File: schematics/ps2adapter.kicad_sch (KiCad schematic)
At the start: 8 parts, among them J14 PS/2, J15 port, U12 CD74HCT299E, U13 CD74HCT299E, U14 SN74LS14N

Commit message: Fix errors in schematics
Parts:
- removed C6: CAP, symbol pspice:CAP
- removed D8: DIODE, symbol pspice:DIODE
- added C2: C, symbol Device:C
- added D8: D, symbol Device:D
- renumbered J14 to J12, J15 to J13
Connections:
- net GND: now also C2.2
- net at R14.1, U14.2 (1Y): now also D8.2 (A)
- net at R14.2, U14.3 (2A): now also C2.1, D8.1 (K)

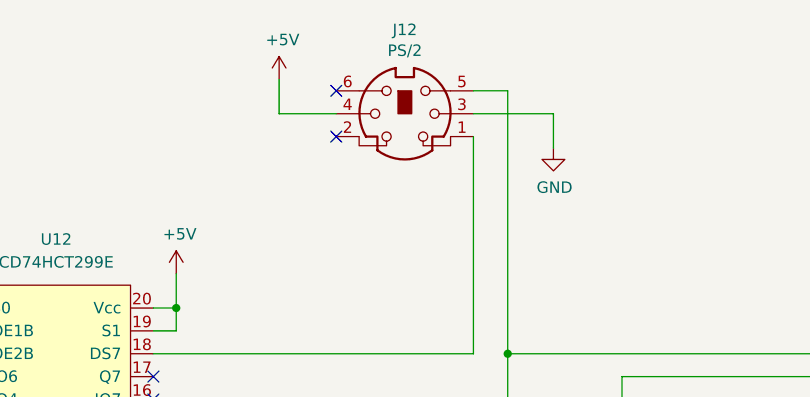
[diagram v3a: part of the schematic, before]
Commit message: Update schematics for latest KiCad
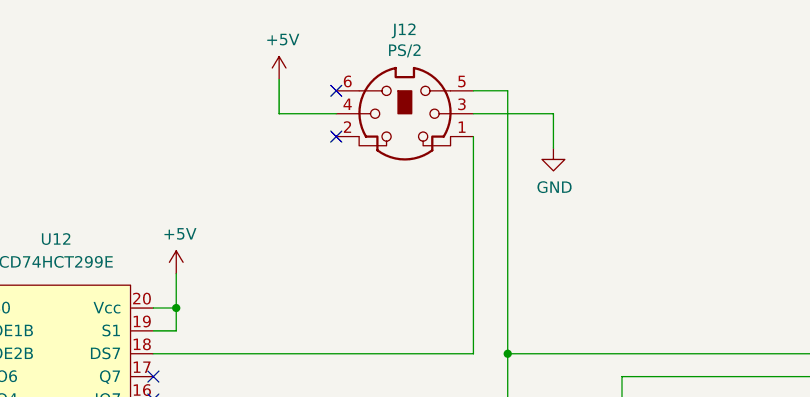
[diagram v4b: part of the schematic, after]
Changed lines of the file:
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@@
 (kicad_sch
-	(version 20231120)
+	(version 20250114)
 	(generator "eeschema")
-	(generator_version "8.0")
+	(generator_version "9.0")
 	(paper "A4")
 	(title_block

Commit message: Update schematics pin numbers
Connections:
- net +5V: now also U14.14 (Vcc); no longer U14.8 (Vcc)
